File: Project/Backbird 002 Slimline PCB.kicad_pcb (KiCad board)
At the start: 2 copper layers, 14 x 116 mm, 8 parts

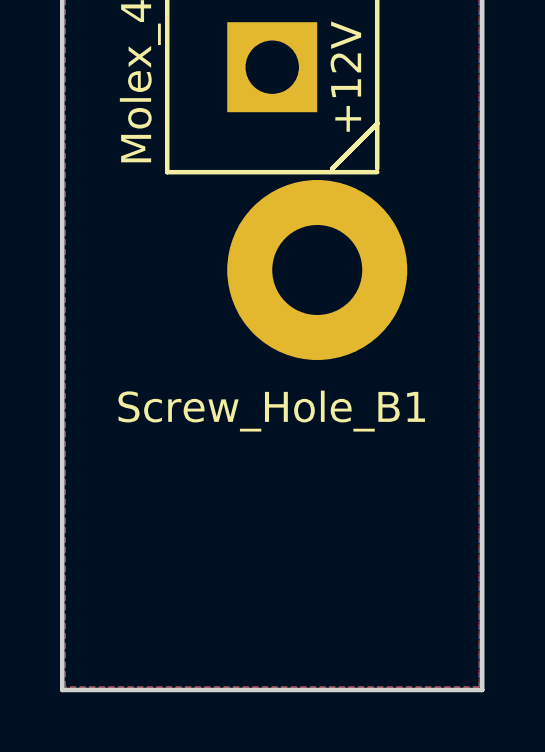
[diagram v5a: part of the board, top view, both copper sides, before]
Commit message: Moved bottom screw hole into correct position
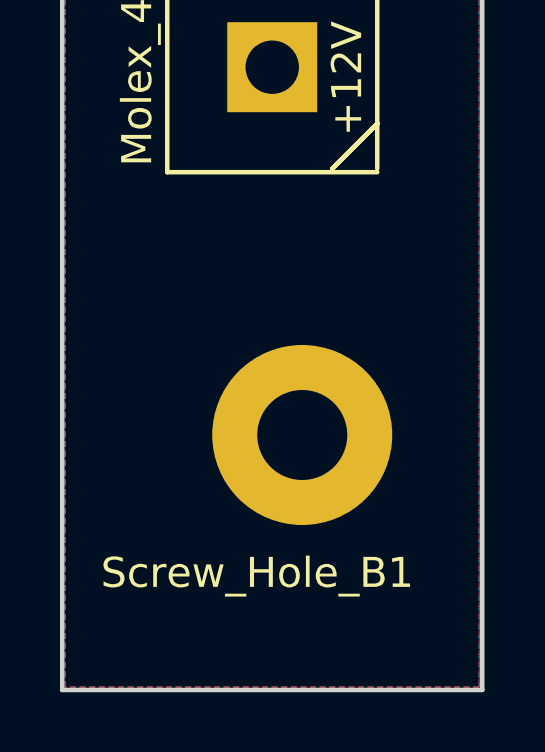
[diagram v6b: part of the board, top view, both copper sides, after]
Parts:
- moved Screw_Hole_B1 5.52 mm to (108.3, 138.0)
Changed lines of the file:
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@@
   (general
     (thickness 1.6)
-    (drawings 24)
+    (drawings 26)
     (tracks 60)
     (zones 0)
@@
     (40 Dwgs.User user)
     (41 Cmts.User user)
-    (42 Eco1.User user hide)
-    (43 Eco2.User user hide)
+    (42 Eco1.User user)
+    (43 Eco2.User user)
     (44 Edge.Cuts user)
     (45 Margin user)
@@
   )
   (module ProjectFootprints:Blackbird002_Slimline_PCB_Screw (layer F.Cu)
-    (at 108.8 132.48)
+    (at 108.3 137.98)
     (fp_text reference Screw_Hole_B1 (at -1.5 4.6) (layer F.SilkS)
       (effects (font (size 1 1) (thickness 0.15)))
@@
     (pad 1 thru_hole oval (at 0 0 90) (size 7 6) (drill oval 4 3) (layers *.Cu *.Mask)
       (net 11 "Net-(Screw_Hole_T1-Pad1)"))
+  )
+  (dimension 5 (width 0.3) (layer Eco1.User)
+    (gr_text "5.000 mm" (at 111.8 152.08) (layer Eco1.User)
+      (effects (font (size 1.5 1.5) (thickness 0.3)))
+    )
+    (feature1 (pts (xy 109.3 148.48) (xy 109.3 150.566421)))
+    (feature2 (pts (xy 114.3 148.48) (xy 114.3 150.566421)))
+    (crossbar (pts (xy 114.3 149.98) (xy 109.3 149.98)))
+    (arrow1a (pts (xy 109.3 149.98) (xy 110.426504 149.393579)))
+    (arrow1b (pts (xy 109.3 149.98) (xy 110.426504 150.566421)))
+    (arrow2a (pts (xy 114.3 149.98) (xy 113.173496 149.393579)))
+    (arrow2b (pts (xy 114.3 149.98) (xy 113.173496 150.566421)))
+  )
+  (dimension 7 (width 0.3) (layer Eco1.User)
+    (gr_text "7.000 mm" (at 120.985019 142.98 90) (layer Eco1.User)
+      (effects (font (size 1.5 1.5) (thickness 0.3)))
+    )
+    (feature1 (pts (xy 116.385019 139.48) (xy 119.47144 139.48)))
+    (feature2 (pts (xy 116.385019 146.48) (xy 119.47144 146.48)))
+    (crossbar (pts (xy 118.885019 146.48) (xy 118.885019 139.48)))
+    (arrow1a (pts (xy 118.885019 139.48) (xy 119.47144 140.606504)))
+    (arrow1b (pts (xy 118.885019 139.48) (xy 118.298598 140.606504)))
+    (arrow2a (pts (xy 118.885019 146.48) (xy 119.47144 145.353496)))
+    (arrow2b (pts (xy 118.885019 146.48) (xy 118.298598 145.353496)))
   )
   (gr_text "ZXJ001 2018\nBlackbird 002\n\nSATA Slimline Backplane\nREV 0.2" (at 107.6 72.68 90) (layer F.SilkS)
@@
   )
   (dimension 7 (width 0.3) (layer Eco1.User)
-    (gr_text "7.000 mm" (at 103.8 154.58) (layer Eco1.User)
-      (effects (font (size 1.5 1.5) (thickness 0.3)))
-    )
-    (feature1 (pts (xy 107.3 148.48) (xy 107.3 153.066421)))
-    (feature2 (pts (xy 100.3 148.48) (xy 100.3 153.066421)))
-    (crossbar (pts (xy 100.3 152.48) (xy 107.3 152.48)))
-    (arrow1a (pts (xy 107.3 152.48) (xy 106.173496 153.066421)))
-    (arrow1b (pts (xy 107.3 152.48) (xy 106.173496 151.893579)))
-    (arrow2a (pts (xy 100.3 152.48) (xy 101.426504 153.066421)))
-    (arrow2b (pts (xy 100.3 152.48) (xy 101.426504 151.893579)))
+    (gr_text "7.000 mm" (at 103.8 158.595077) (layer Eco1.User)
+      (effects (font (size 1.5 1.5) (thickness 0.3)))
+    )
+    (feature1 (pts (xy 107.3 154.49863) (xy 107.3 157.081498)))
+    (feature2 (pts (xy 100.3 154.49863) (xy 100.3 157.081498)))
+    (crossbar (pts (xy 100.3 156.495077) (xy 107.3 156.495077)))
+    (arrow1a (pts (xy 107.3 156.495077) (xy 106.173496 157.081498)))
+    (arrow1b (pts (xy 107.3 156.495077) (xy 106.173496 155.908656)))
+    (arrow2a (pts (xy 100.3 156.495077) (xy 101.426504 157.081498)))
+    (arrow2b (pts (xy 100.3 156.495077) (xy 101.426504 155.908656)))
   )
   (gr_line (start 100.3 146.48) (end 114.3 146.48) (layer Eco1.User) (width 0.2))
